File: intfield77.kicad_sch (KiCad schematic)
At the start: 20 parts, among them J1 USB_C_Receptacle, SW1 RESET, SW2 BOOT, U1 STM32F072C8Tx, U2 SRV05-4, U3 XC6206PxxxMR

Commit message: First routing of the PCB except the matrices.
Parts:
- R1, R2, R3: footprint Resistor_SMD:R_0815_2038Metric -> Resistor_SMD:R_0805_2012Metric
- U2: footprint Package_TO_SOT_SMD:SOT-23-6 -> marbastlib-various:SOT-23-6-routable
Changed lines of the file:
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@@
       (effects (font (size 1.27 1.27)) (justify left))
     )
-    (property "Footprint" "Resistor_SMD:R_0815_2038Metric" (at 48.26 67.31 0)
+    (property "Footprint" "Resistor_SMD:R_0805_2012Metric" (at 48.26 67.31 0)
       (effects (font (size 1.27 1.27)) hide)
     )
@@
       (effects (font (size 1.27 1.27)) (justify left))
     )
-    (property "Footprint" "Resistor_SMD:R_0815_2038Metric" (at 46.99 176.53 0)
+    (property "Footprint" "Resistor_SMD:R_0805_2012Metric" (at 46.99 176.53 0)
       (effects (font (size 1.27 1.27)) hide)
     )
@@
       (effects (font (size 1.27 1.27)) (justify left))
     )
-    (property "Footprint" "Resistor_SMD:R_0815_2038Metric" (at 58.42 67.31 0)
+    (property "Footprint" "Resistor_SMD:R_0805_2012Metric" (at 58.42 67.31 0)
       (effects (font (size 1.27 1.27)) hide)
     )
@@
       (effects (font (size 1.27 1.27)) (justify left))
     )
-    (property "Footprint" "Package_TO_SOT_SMD:SOT-23-6" (at 275.59 63.5 0)
-      (effects (font (size 1.27 1.27)) hide)
-    )
+    (property "Footprint" "marbastlib-various:SOT-23-6-routable" (at 275.59 63.5 0)
+      (effects (font (size 1.27 1.27)) hide)
+    )

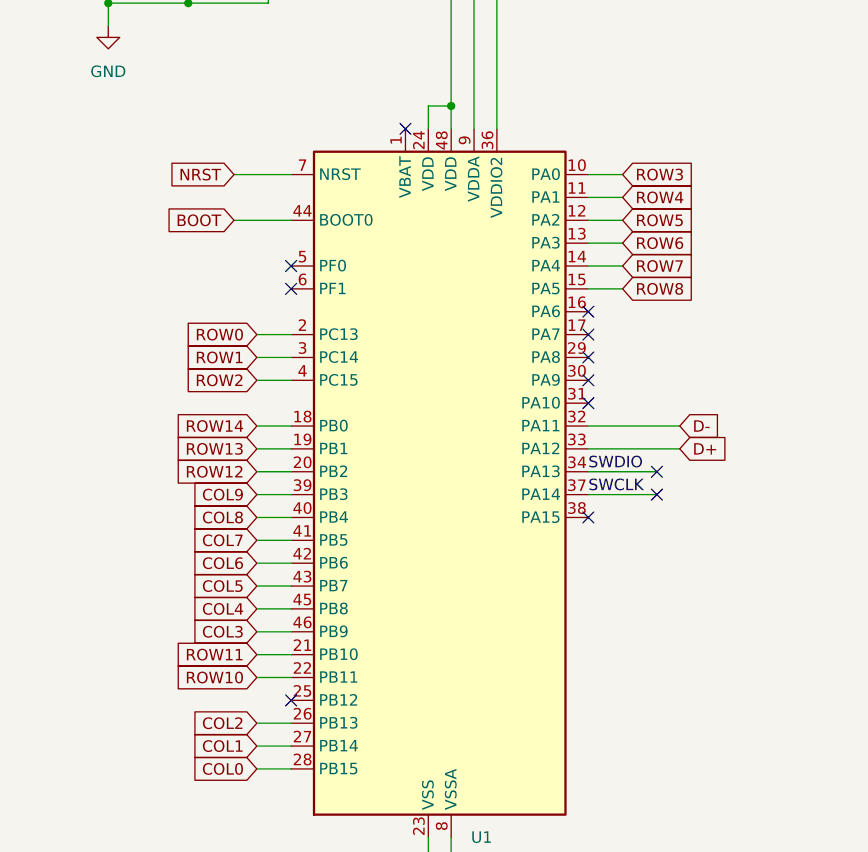
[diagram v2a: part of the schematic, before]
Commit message: Reassigned pins and complete routing.
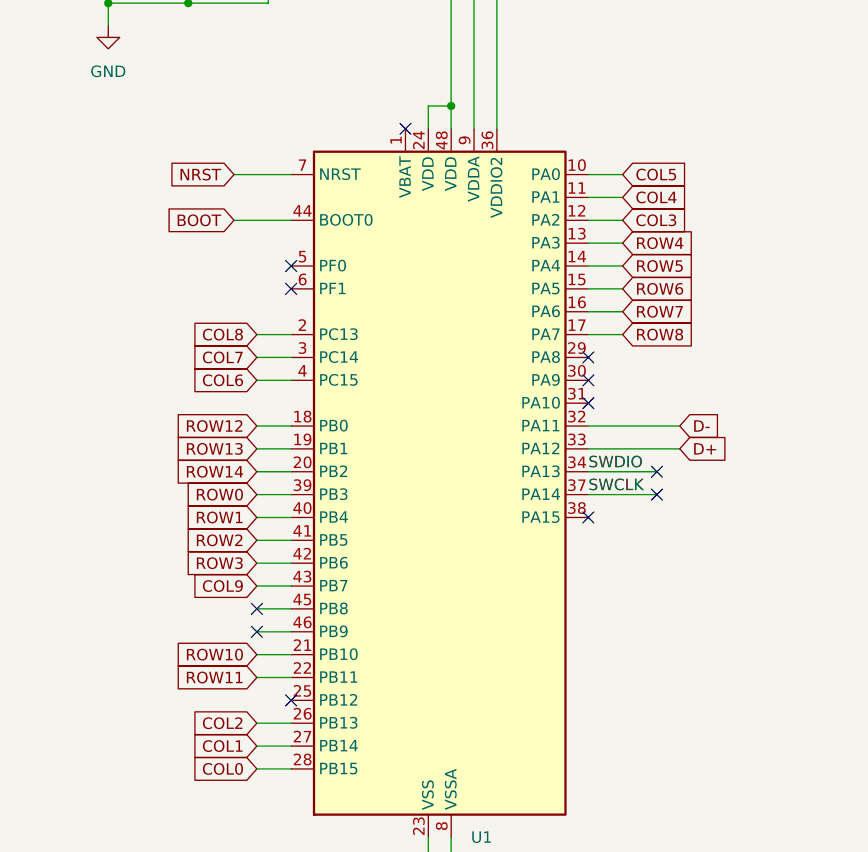
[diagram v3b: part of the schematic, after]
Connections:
- net COL3: now also U1.12 (PA2); no longer U1.46 (PB9)
- net COL4: now also U1.11 (PA1); no longer U1.45 (PB8)
- net COL5: now also U1.10 (PA0); no longer U1.43 (PB7)
- net COL6: now also U1.4 (PC15); no longer U1.42 (PB6)
- net COL7: now also U1.3 (PC14); no longer U1.41 (PB5)
- net COL8: now also U1.2 (PC13); no longer U1.40 (PB4)
- net COL9: now also U1.43 (PB7); no longer U1.39 (PB3)
- net ROW0: now also U1.39 (PB3); no longer U1.2 (PC13)
- net ROW1: now also U1.40 (PB4); no longer U1.3 (PC14)
- net ROW10: now also U1.21 (PB10); no longer U1.22 (PB11)
- net ROW11: now also U1.22 (PB11); no longer U1.21 (PB10)
- net ROW12: now also U1.18 (PB0); no longer U1.20 (PB2)
- net ROW14: now also U1.20 (PB2); no longer U1.18 (PB0)
- net ROW2: now also U1.41 (PB5); no longer U1.4 (PC15)
- net ROW3: now also U1.42 (PB6); no longer U1.10 (PA0)
- net ROW4: now also U1.13 (PA3); no longer U1.11 (PA1)
- net ROW5: now also U1.14 (PA4); no longer U1.12 (PA2)
- net ROW6: now also U1.15 (PA5); no longer U1.13 (PA3)
- net ROW7: now also U1.16 (PA6); no longer U1.14 (PA4)
- net ROW8: now also U1.17 (PA7); no longer U1.15 (PA5)
